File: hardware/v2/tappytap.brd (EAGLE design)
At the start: 36 x 13.4 mm, 18 parts

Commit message: Finished routing on first pass
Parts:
- moved C1 1.00 mm to (6.00, 13.0)
- moved C2 1.00 mm to (10.0, 13.0)
- moved C3 1.00 mm to (26.0, 13.0)
- moved C4 1.00 mm to (30.0, 13.0)
- moved DATA_IN 1.00 mm to (2.00, 2.60)
- moved DATA_OUT 1.00 mm to (34.0, 2.60)
- moved HBR1 1.00 mm to (8.00, 7.00)
- moved HBR2 1.00 mm to (18.0, 7.00)
- moved HBR3 1.00 mm to (28.0, 7.00)
- moved S1 1.00 mm to (10.0, 11.7)
- moved S2 1.00 mm to (10.0, 7.70)
- moved S3 1.00 mm to (10.0, 3.70)
- moved S4 1.00 mm to (18.0, 11.7)
- moved S5 1.00 mm to (18.0, 7.70)
- moved S6 1.00 mm to (18.0, 3.70)
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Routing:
- net GND: track 87.8 -> 131.6 mm
- net SCK: track 44.2 -> 60.4 mm
- net S6A: track 0.00 -> 13.5 mm, vias 0 -> 1
- net S9A: track 0.00 -> 13.5 mm, vias 0 -> 1
- net NCV_CS: track 44.4 -> 55.7 mm
- net S2A: track 0.00 -> 11.0 mm, vias 0 -> 1
- net S2B: track 0.00 -> 8.44 mm, vias 0 -> 1
- net S5B: track 0.00 -> 7.93 mm, vias 0 -> 1
- net S8B: track 0.00 -> 7.47 mm, vias 0 -> 1
- net S3A: track 7.53 -> 14.7 mm
- net S8A: track 0.00 -> 6.83 mm, vias 0 -> 1
- net N$26: track 12.1 -> 18.5 mm
- net S5A: track 0.00 -> 5.55 mm, vias 0 -> 1
- net +5V: track 101.1 -> 105.7 mm, vias 1 -> 2
- net S9B: track 7.66 -> 3.56 mm
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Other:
- board size 36 x 13.4 mm -> 36 x 15 mm

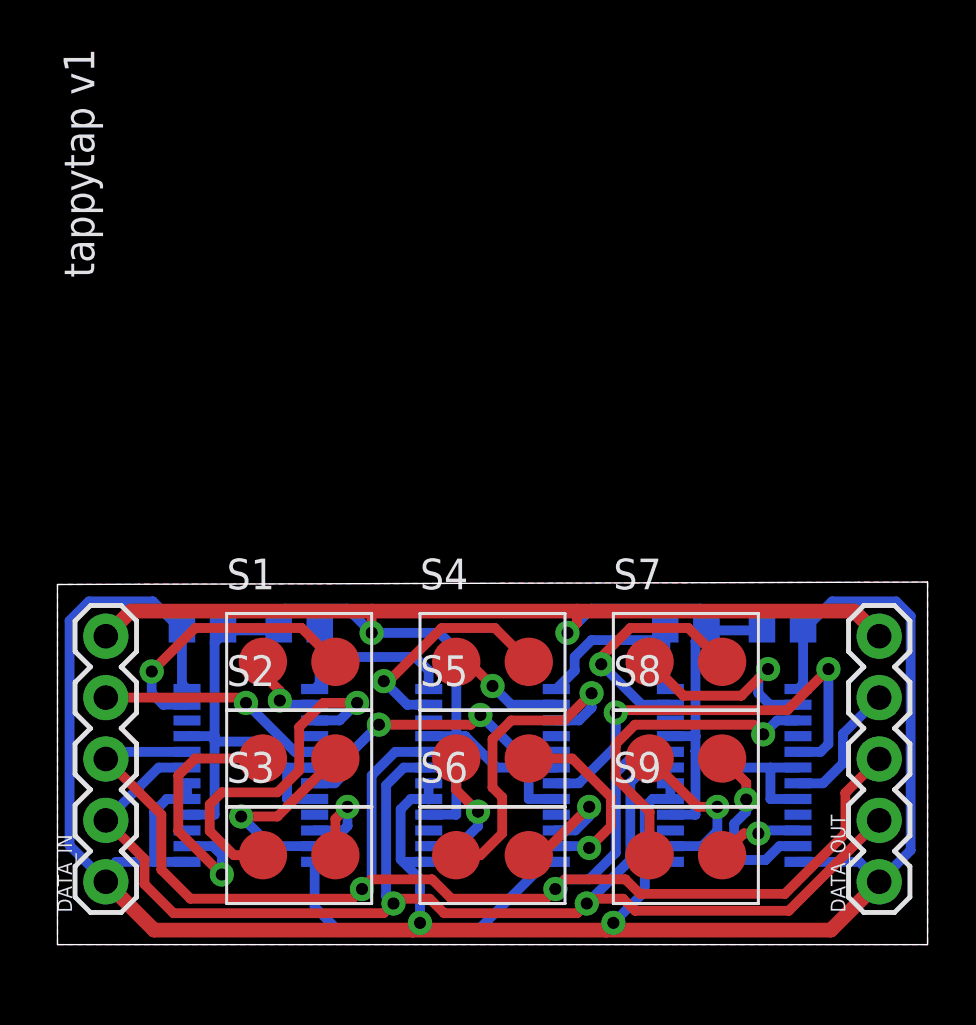
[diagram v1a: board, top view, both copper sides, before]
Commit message: Finalize routing
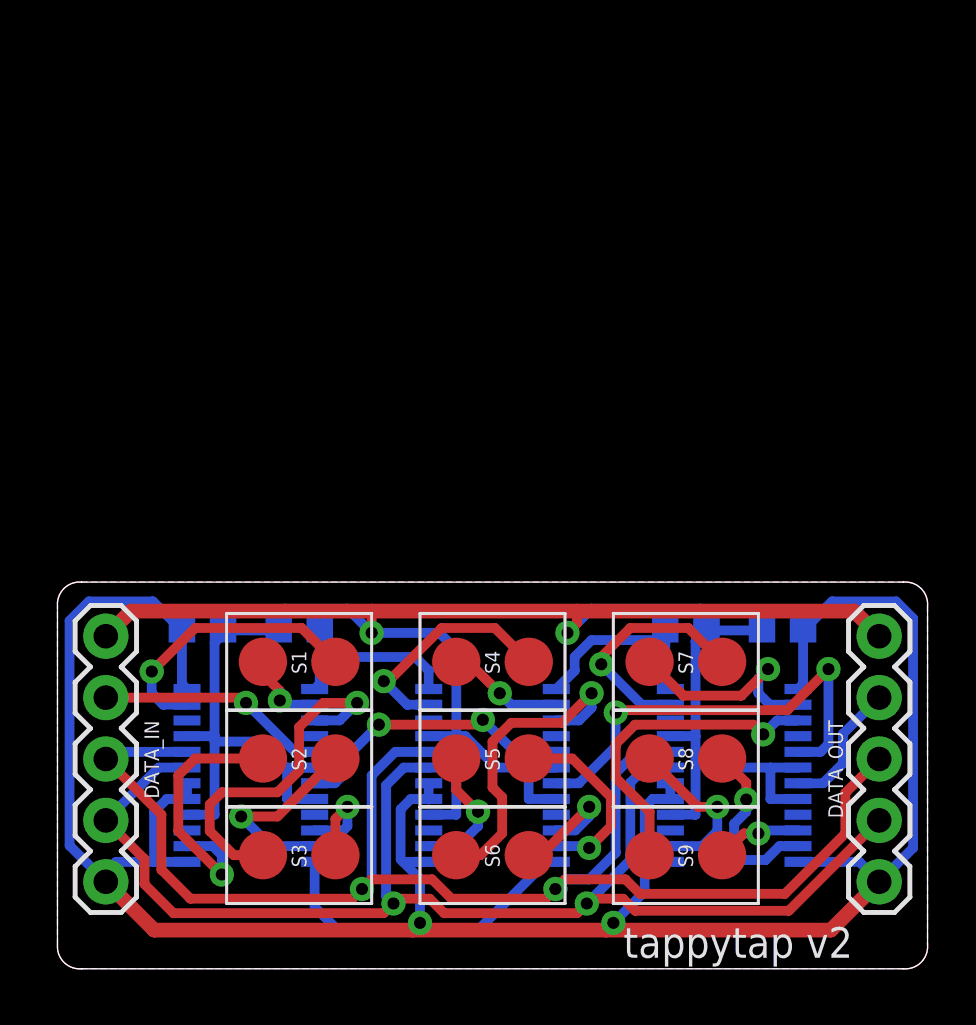
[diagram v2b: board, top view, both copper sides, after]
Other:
- board size 36 x 15 mm -> 36 x 16 mm
- board text added: "tappytap v2"
- board text removed: "tappytap v1"

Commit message: Final with gerbers for v2
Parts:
- moved C1 0.10 mm to (5.90, 13.0)
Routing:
- net GND: track 131.7 -> 156.9 mm, vias 2 -> 4
- net S1B: track 11.5 -> 12.5 mm
- net +5V: track 105.7 -> 106.3 mm
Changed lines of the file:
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@@
 <layer number="14" name="Route14" color="1" fill="6" visible="no" active="no"/>
 <layer number="15" name="Route15" color="4" fill="6" visible="no" active="no"/>
-<layer number="16" name="Bottom" color="1" fill="1" visible="no" active="yes"/>
+<layer number="16" name="Bottom" color="1" fill="1" visible="yes" active="yes"/>
 <layer number="17" name="Pads" color="2" fill="1" visible="yes" active="yes"/>
 <layer number="18" name="Vias" color="2" fill="1" visible="yes" active="yes"/>
@@
 <layer number="20" name="Dimension" color="15" fill="1" visible="yes" active="yes"/>
 <layer number="21" name="tPlace" color="7" fill="1" visible="yes" active="yes"/>
-<layer number="22" name="bPlace" color="7" fill="1" visible="no" active="yes"/>
+<layer number="22" name="bPlace" color="7" fill="1" visible="yes" active="yes"/>
 <layer number="23" name="tOrigins" color="15" fill="1" visible="yes" active="yes"/>
-<layer number="24" name="bOrigins" color="15" fill="1" visible="no" active="yes"/>
+<layer number="24" name="bOrigins" color="15" fill="1" visible="yes" active="yes"/>
 <layer number="25" name="tNames" color="7" fill="1" visible="yes" active="yes"/>
-<layer number="26" name="bNames" color="7" fill="1" visible="no" active="yes"/>
+<layer number="26" name="bNames" color="7" fill="1" visible="yes" active="yes"/>
 <layer number="27" name="tValues" color="7" fill="1" visible="no" active="yes"/>
 <layer number="28" name="bValues" color="7" fill="1" visible="no" active="yes"/>
@@
 <layer number="38" name="bTest" color="7" fill="1" visible="no" active="yes"/>
 <layer number="39" name="tKeepout" color="4" fill="11" visible="yes" active="yes"/>
-<layer number="40" name="bKeepout" color="1" fill="11" visible="no" active="yes"/>
+<layer number="40" name="bKeepout" color="1" fill="11" visible="yes" active="yes"/>
 <layer number="41" name="tRestrict" color="4" fill="10" visible="yes" active="yes"/>
-<layer number="42" name="bRestrict" color="1" fill="10" visible="no" active="yes"/>
+<layer number="42" name="bRestrict" color="1" fill="10" visible="yes" active="yes"/>
 <layer number="43" name="vRestrict" color="2" fill="10" visible="no" active="yes"/>
 <layer number="44" name="Drills" color="7" fill="1" visible="yes" active="yes"/>
@@
 <layer number="49" name="Reference" color="7" fill="1" visible="yes" active="yes"/>
 <layer number="50" name="dxf" color="7" fill="1" visible="no" active="no"/>
-<layer number="51" name="tDocu" color="7" fill="1" visible="no" active="yes"/>
-<layer number="52" name="bDocu" color="7" fill="1" visible="no" active="yes"/>
+<layer number="51" name="tDocu" color="7" fill="1" visible="yes" active="yes"/>
+<layer number="52" name="bDocu" color="7" fill="1" visible="yes" active="yes"/>
 <layer number="53" name="tGND_GNDA" color="7" fill="9" visible="no" active="no"/>
 <layer number="54" name="bGND_GNDA" color="1" fill="9" visible="no" active="no"/>
@@
 <layer number="118" name="Rect_Pads" color="7" fill="1" visible="no" active="yes"/>
 <layer number="121" name="_tsilk" color="7" fill="1" visible="yes" active="yes"/>
-<layer number="122" name="_bsilk" color="7" fill="1" visible="no" active="yes"/>
+<layer number="122" name="_bsilk" color="7" fill="1" visible="yes" active="yes"/>
 <layer number="123" name="tTestmark" color="7" fill="1" visible="no" active="yes"/>
 <layer number="124" name="bTestmark" color="7" fill="1" visible="no" active="yes"/>
@@
 </autorouter>
 <elements>
-<element name="C1" library="rcl" package="C0603" value="10uF" x="6" y="13" smashed="yes" rot="MR0">
-<attribute name="NAME" x="6.53" y="13.684" size="0.6096" layer="26" font="vector" ratio="15" rot="MR0"/>
-<attribute name="VALUE" x="6.635" y="11.095" size="0.6096" layer="28" font="vector" ratio="15" rot="MR0"/>
+<element name="C1" library="rcl" package="C0603" value="10uF" x="5.9" y="13" smashed="yes" rot="MR0">
+<attribute name="NAME" x="6.43" y="13.684" size="0.6096" layer="26" font="vector" ratio="15" rot="MR0"/>
+<attribute name="VALUE" x="6.535" y="11.095" size="0.6096" layer="28" font="vector" ratio="15" rot="MR0"/>
 </element>
 <element name="HBR1" library="Sparky" package="24-SSOP" value="NCV7718" x="8" y="7" smashed="yes" rot="MR0">
@@
 <wire x1="21.48940625" y1="13.8" x2="32.96" y2="13.8" width="0.6096" layer="1"/>
 <wire x1="32.96" y1="13.8" x2="34" y2="12.76" width="0.6096" layer="1"/>
-<wire x1="6.85" y1="13" x2="7" y2="13" width="0.4064" layer="16"/>
-<wire x1="7" y1="13" x2="9.15" y2="13" width="0.4064" layer="16"/>
 <wire x1="29.15" y1="13" x2="26.85" y2="13" width="0.4064" layer="16"/>
 <contactref element="HBR1" pad="21"/>
@@
 <wire x1="13" y1="12.9" x2="13" y2="13.8" width="0.4064" layer="1"/>
 <wire x1="26.6" y1="12.75" x2="26.85" y2="13" width="0.4064" layer="16"/>
-<wire x1="7" y1="13" x2="6.5" y2="12.5" width="0.4064" layer="16"/>
-<wire x1="6.5" y1="12.5" x2="6.5" y2="8.625" width="0.4064" layer="16"/>
 <wire x1="6.5" y1="8.625" x2="6.5" y2="8.4" width="0.4064" layer="16"/>
 <wire x1="6.5" y1="8.4" x2="6.5" y2="5.375" width="0.4064" layer="16"/>
@@
 <wire x1="26.8" y1="13.7" x2="26.8" y2="13.05" width="0.4064" layer="16"/>
 <wire x1="26.8" y1="13.05" x2="26.85" y2="13" width="0.4064" layer="16"/>
+<wire x1="6.65" y1="12.95" x2="5.8" y2="12.1" width="0.4064" layer="16"/>
+<wire x1="5.8" y1="12.1" x2="5.8" y2="11.5" width="0.4064" layer="16"/>
+<wire x1="5.8" y1="11.5" x2="6.5" y2="10.8" width="0.4064" layer="16"/>
+<wire x1="6.5" y1="10.8" x2="6.5" y2="8.625" width="0.4064" layer="16"/>
+<wire x1="6.75" y1="13" x2="6.7" y2="12.95" width="0.4064" layer="16"/>
+<wire x1="6.7" y1="12.95" x2="6.65" y2="12.95" width="0.4064" layer="16"/>
+<wire x1="9.15" y1="13" x2="6.75" y2="13" width="0.4064" layer="16"/>
 </signal>
 <signal name="GND" class="2">
@@
 <contactref element="DATA_IN" pad="1"/>
 <contactref element="DATA_OUT" pad="1"/>
-<wire x1="5.36" y1="10.575" x2="5.15" y2="10.785" width="0.4064" layer="16"/>
-<wire x1="5.15" y1="10.785" x2="5.15" y2="13" width="0.4064" layer="16"/>
 <wire x1="2" y1="3" x2="2" y2="2.6" width="0.4064" layer="16"/>
 <wire x1="5.36" y1="3.425" x2="4" y2="3.425" width="0.4064" layer="16"/>
@@
 <wire x1="15.36" y1="10.575" x2="15.36" y2="11.34" width="0.4064" layer="16"/>
 <wire x1="15.36" y1="11.34" x2="14.8" y2="11.9" width="0.4064" layer="16"/>
-<wire x1="14.8" y1="11.9" x2="10.95" y2="11.9" width="0.4064" layer="16"/>
+<wire x1="14.8" y1="11.9" x2="11" y2="11.9" width="0.4064" layer="16"/>
+<wire x1="11" y1="11.9" x2="10.95" y2="11.9" width="0.4064" layer="16"/>
 <wire x1="10.95" y1="11.9" x2="10.85" y2="12" width="0.4064" layer="16"/>
 <wire x1="14.625" y1="6.025" x2="14.2" y2="5.6" width="0.4064" layer="16"/>
@@
 <wire x1="24.3" y1="3.425" x2="24.3" y2="2.2" width="0.4064" layer="16"/>
 <wire x1="24.3" y1="2.2" x2="23" y2="0.9" width="0.4064" layer="16"/>
-<wire x1="5.15" y1="13" x2="3.95" y2="14.2" width="0.4064" layer="16"/>
 <wire x1="3.95" y1="14.2" x2="1.3" y2="14.2" width="0.4064" layer="16"/>
 <wire x1="1.3" y1="14.2" x2="0.5" y2="13.4" width="0.4064" layer="16"/>
@@
 <vertex x="0" y="0"/>
 </polygon>
+<wire x1="21.4" y1="11.9" x2="19.1" y2="11.9" width="0.4064" layer="16"/>
+<wire x1="19.1" y1="11.9" x2="16.5" y2="14.5" width="0.4064" layer="16"/>
+<wire x1="16.5" y1="14.5" x2="4.3" y2="14.5" width="0.4064" layer="16"/>
+<wire x1="4.3" y1="14.5" x2="4" y2="14.2" width="0.4064" layer="16"/>
+<wire x1="5.36" y1="10.575" x2="5.125" y2="10.575" width="0.4064" layer="16"/>
+<wire x1="5.125" y1="10.575" x2="4.8" y2="10.9" width="0.4064" layer="16"/>
+<wire x1="4.8" y1="10.9" x2="4.8" y2="11.9" width="0.4064" layer="16"/>
+<wire x1="4.8" y1="11.9" x2="4.8" y2="12.5" width="0.4064" layer="16"/>
+<wire x1="4.8" y1="12.5" x2="5.2" y2="12.9" width="0.4064" layer="16"/>
+<via x="6.8" y="11.8" extent="1-16" drill="0.5" shape="octagon"/>
+<wire x1="6.8" y1="11.8" x2="10.9" y2="11.8" width="0.4064" layer="16"/>
+<wire x1="10.9" y1="11.8" x2="11" y2="11.9" width="0.4064" layer="16"/>
+<wire x1="5.05" y1="13" x2="5.05" y2="13.15" width="0.4064" layer="16"/>
+<wire x1="5.05" y1="13.15" x2="4" y2="14.2" width="0.4064" layer="16"/>
+<wire x1="6.8" y1="11.8" x2="4.9" y2="11.8" width="0.4064" layer="1"/>
+<wire x1="4.9" y1="11.8" x2="4.8" y2="11.9" width="0.4064" layer="1"/>
+<via x="4.8" y="11.9" extent="1-16" drill="0.5" shape="octagon"/>
 </signal>
 <signal name="SCK">
@@
 <contactref element="S1" pad="P$2"/>
 <wire x1="11.5" y1="11.7" x2="10.1" y2="13.1" width="0.4064" layer="1"/>
-<wire x1="10.1" y1="13.1" x2="5.7" y2="13.1" width="0.4064" layer="1"/>
-<wire x1="5.7" y1="13.1" x2="3.9" y2="11.3" width="0.4064" layer="1"/>
-<via x="3.9" y="11.3" extent="1-16" drill="0.5" shape="octagon"/>
-<wire x1="3.9" y1="11.3" x2="3.9" y2="10.4" width="0.4064" layer="16"/>
-<wire x1="3.9" y1="10.4" x2="4.375" y2="9.925" width="0.4064" layer="16"/>
+<wire x1="10.1" y1="13.1" x2="4.5" y2="13.1" width="0.4064" layer="1"/>
+<via x="3.5" y="11.5" extent="1-16" drill="0.5" shape="octagon"/>
+<wire x1="3.5" y1="11.5" x2="3.5" y2="10.8" width="0.4064" layer="16"/>
+<wire x1="3.5" y1="10.8" x2="4.375" y2="9.925" width="0.4064" layer="16"/>
 <wire x1="4.375" y1="9.925" x2="5.36" y2="9.925" width="0.4064" layer="16"/>
+<wire x1="3.5" y1="11.5" x2="3.5" y2="12.1" width="0.4064" layer="1"/>
+<wire x1="3.5" y1="12.1" x2="4.5" y2="13.1" width="0.4064" layer="1"/>
 </signal>
 <signal name="S2A">
